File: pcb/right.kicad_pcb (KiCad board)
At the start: 2 copper layers, 210.9 x 125.7 mm, 95 parts, among them K1 KEY_GRV, K10 KEY_N, K11 KEY_TR2, K12 KEY_U, K13 KEY_J, K14 KEY_M, K15 KEY_TR3, K16 KEY_9, K17 KEY_I, K18 KEY_K, K19 KEY_COMM, K2 KEY_7, K20 KEY_FN, K21 KEY_0, K22 KEY_O, K23 KEY_L, K24 KEY_PER, K25 KEY_RCTL, K26 KEY_MIN, K27 KEY_P, K28 KEY_COLN, K29 KEY_SLSH, K3 KEY_8, K30 KEY_LEFT, K31 KEY_PLS, K32 KEY_LBR, K33 KEY_QUOT, K34 KEY_RSFT, K35 KEY_DOWN, K36 KEY_BSPC, K37 KEY_RBR, K38 KEY_ENT, K39 KEY_UP, K4 KEY_CR1, K40 KEY_RGHT, K41 KEY_BSLS, K42 KEY_RR1, K43 KEY_RR2, K5 KEY_CR2, K6 KEY_CR3, K7 KEY_TR1, K8 KEY_Y, K9 KEY_H, U1 TRRS, U2 ProMicro

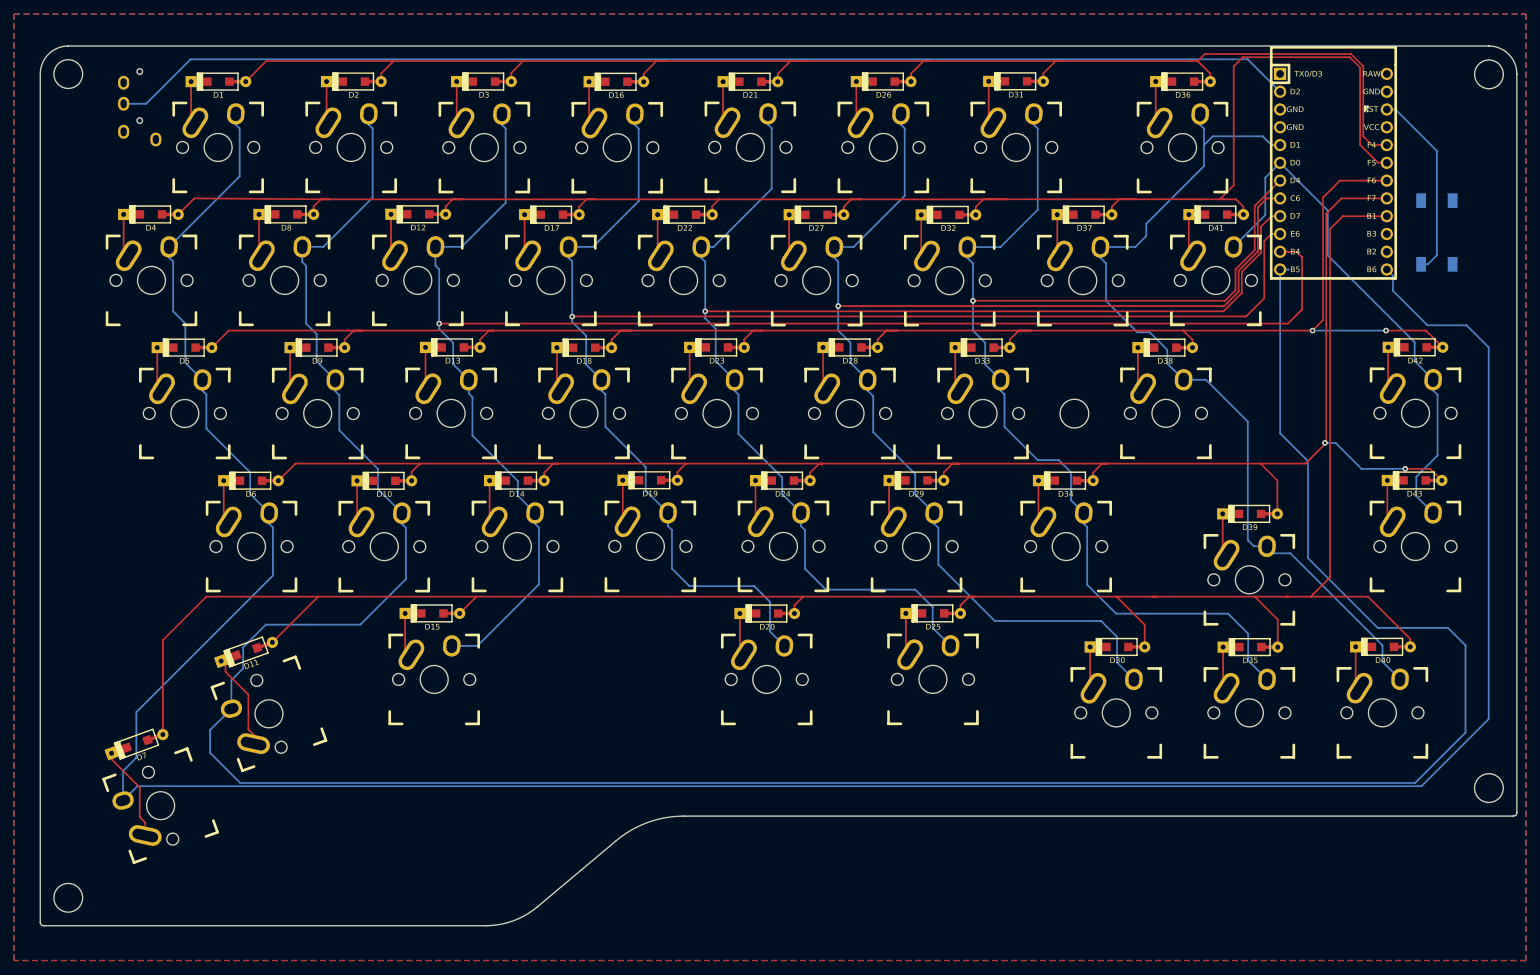
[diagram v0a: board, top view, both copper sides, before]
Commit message: Trying to add some fillets but something is messed up
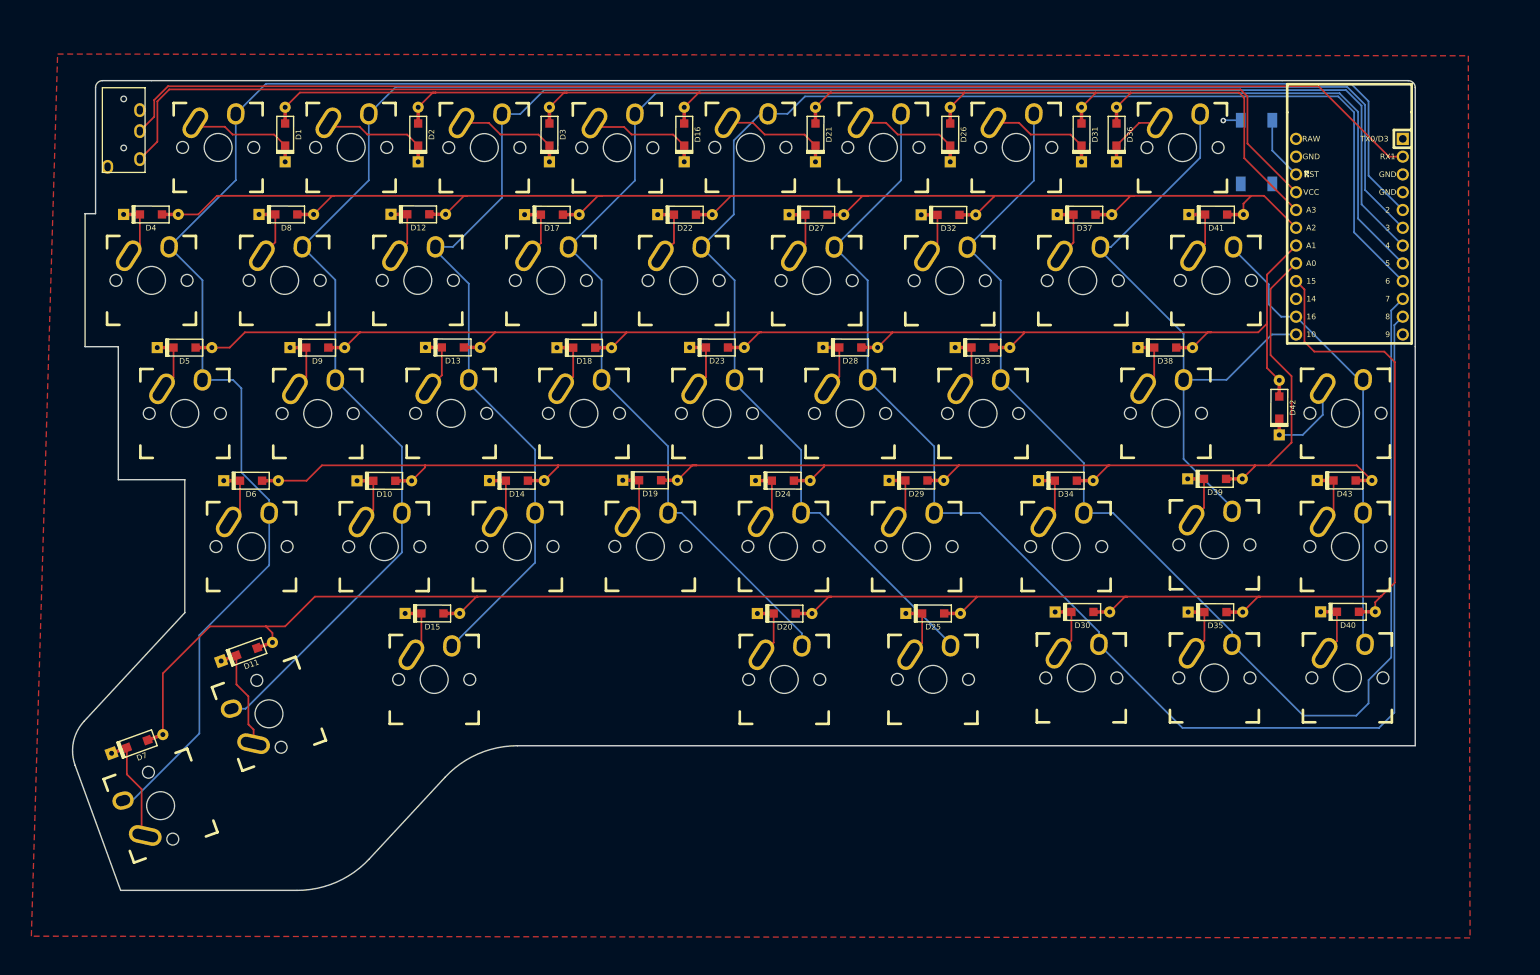
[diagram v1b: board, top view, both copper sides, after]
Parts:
- removed  : MountingHole_4mm, MountingHole:MountingHole_4mm (x5)
- U1: moved to F.Cu
- U2: value ProMicro -> ProMicro USBC; footprint keebio:ArduinoProMicro -> keebio:ArduinoProMicro-USBC-Alibaba; moved to B.Cu
- moved S1 28.2 mm to (193.5, 35.0), turned to 90 degrees
- moved D42 21.3 mm to (196.8, 71.5), turned to 90 degrees
- moved D16 12.3 mm to (111.8, 32.5), turned to 90 degrees
- moved D1 12.2 mm to (54.8, 32.5), turned to 90 degrees
- moved D26 12.2 mm to (149.8, 32.5), turned to 90 degrees
- moved D36 12.1 mm to (173.5, 32.5), turned to 90 degrees
- moved D31 12.0 mm to (168.5, 32.5), turned to 90 degrees
- moved D3 12.0 mm to (92.5, 32.5), turned to 90 degrees
- moved D21 12.0 mm to (130.5, 32.5), turned to 90 degrees
- moved D2 11.9 mm to (73.8, 32.5), turned to 90 degrees
- moved D43 10.0 mm to (206.1, 81.9)
- moved K42 10.0 mm to (206.2, 72.3)
- moved K43 10.0 mm to (206.2, 91.3)
- moved U2 9.55 mm to (206.8, 47.1)
- moved D30 7.07 mm to (168.6, 100.7)
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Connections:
- net /GND renamed GND
- net /VCC renamed VCC
- K40 pad 2: /col7 -> /col8
- S1 pad 1: Net-(S1-Pad1) -> unconnected-(S1-Pad1)
- S1 pad 3: Net-(S1-Pad3) -> unconnected-(S1-Pad3)
- U1 pad 4: Net-(U1-Pad4) -> unconnected-(U1-Pad4)
- U2 pad 1: Net-(U2-Pad1) -> unconnected-(U2-Pad1)
- U2 pad 10: /col3 -> /col6
- U2 pad 11: /col2 -> /col5
- U2 pad 12: /col1 -> unconnected-(U2-Pad12)
- U2 pad 13: /col0 -> /col7
- U2 pad 14: Net-(U2-Pad14) -> /col8
- U2 pad 15: Net-(U2-Pad15) -> unconnected-(U2-Pad15)
- U2 pad 24: Net-(U2-Pad24) -> unconnected-(U2-Pad24)
- U2 pad 5: /col7 -> /col0
- U2 pad 6: /col8 -> /col1
- U2 pad 7: /col6 -> /col2
- U2 pad 8: /col5 -> /col3
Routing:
- net VCC: track 0.00 -> 182.7 mm
- net /col1: track 391.3 -> 270.8 mm
- net /col0: track 390.9 -> 302.1 mm
- net /row1: track 238.6 -> 195.1 mm
- net /row2: track 236.5 -> 196.2 mm, vias 2 -> 0
- net /col7: track 125.0 -> 90.0 mm
- net /row4: track 298.0 -> 267.6 mm
- net /row3: track 242.0 -> 212.6 mm, vias 2 -> 0
- net /row0: track 207.1 -> 179.0 mm
- net /serial: track 169.7 -> 188.6 mm
- net /RST: track 27.3 -> 9.15 mm
- net /col5: track 188.3 -> 204.3 mm, vias 1 -> 0
- net /col4: track 195.3 -> 209.6 mm, vias 1 -> 0
- net /col3: track 211.3 -> 224.7 mm, vias 1 -> 0
- net /col8: track 76.3 -> 66.1 mm
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- added copper zone on F.Cu, net GND
- removed copper zone on B.Cu, net GND
- removed copper zone on F.Cu, net VCC
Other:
- board size 210.9 x 125.7 mm -> 191.8 x 115.7 mm
- net class Default removed

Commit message: This is the version that I sent to manufacturers
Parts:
- moved G*** 27.6 mm to (101.5, 108.2)
- moved U1 1.00 mm to (30.7, 25.8)
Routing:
- net VCC: track 182.7 -> 183.7 mm
- net /serial: track 188.6 -> 189.6 mm
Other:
- board size 191.8 x 115.7 mm -> 191.7 x 116.2 mm
- rule pad_to_mask_clearance: 0.051 -> 0
- board text added: "JLCJLCJLCJLC"
